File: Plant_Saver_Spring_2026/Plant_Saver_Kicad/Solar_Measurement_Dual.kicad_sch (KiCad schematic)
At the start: 9 parts, among them U14 MCP6234

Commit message: Resub from last
I forgot to save some of my changes from my last push
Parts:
- added C15: 0.1uF, Capacitor_THT:C_Disc_D4.7mm_W2.5mm_P5.00mm, symbol Device:C
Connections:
- net Vcc: now also C15.1; no longer U14.4 (V+)
- net Vmeas1: now also U14.1, U14.2 (-)
- new net: C15.2, U14.4 (V+)
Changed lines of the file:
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@@
+	)
+	(junction
+		(at 165.1 50.8)
+		(diameter 0)
+		(color 0 0 0 0)
 	)
 	(junction
@@
 	(wire
 		(pts
+			(xy 93.98 53.34) (xy 97.79 53.34)
+		)
+		(stroke
+			(width 0)
+			(type default)
+		)
+	)
+	(wire
+		(pts
 			(xy 138.43 132.08) (xy 140.97 132.08)
 		)
@@
 	(wire
 		(pts
+			(xy 165.1 50.8) (xy 170.18 50.8)
+		)
+		(stroke
+			(width 0)
+			(type default)
+		)
+	)
+	(wire
+		(pts
 			(xy 115.57 53.34) (xy 115.57 66.04)
 		)
@@
 	(wire
 		(pts
-			(xy 95.25 53.34) (xy 97.79 53.34)
+			(xy 82.55 53.34) (xy 86.36 53.34)
 		)
 		(stroke
@@
 	(hierarchical_label "Vcc"
 		(shape input)
-		(at 95.25 53.34 180)
+		(at 82.55 53.34 180)
 		(effects
 			(font
@@
 					(unit 1)
 				)
+			)
+		)
+	)
+	(symbol
+		(lib_id "Device:C")
+		(at 90.17 53.34 90)
+		(unit 1)
+		(exclude_from_sim no)
+		(in_bom yes)
+		(on_board yes)
+		(dnp no)
+		(property "Reference" "C15"
+			(at 88.9 50.038 0)
+			(effects
+				(font
+					(size 1.27 1.27)
+				)
+				(justify left)
+			)
+		)
+		(property "Value" "0.1uF"
+			(at 91.44 50.038 0)
+			(effects
+				(font
+					(size 1.27 1.27)
+				)
+				(justify left)
+			)
+		)
+		(property "Footprint" "Capacitor_THT:C_Disc_D4.7mm_W2.5mm_P5.00mm"
+			(at 93.98 52.3748 0)
+			(effects
+				(font
+					(size 1.27 1.27)
+				)
+				(hide yes)
+			)
+		)
+		(property "Datasheet" "~"
+			(at 90.17 53.34 0)
+			(effects
+				(font
+					(size 1.27 1.27)
+				)
+				(hide yes)
+			)
+		)
+		(property "Description" "Unpolarized capacitor"
+			(at 90.17 53.34 0)
+			(effects
+				(font
+					(size 1.27 1.27)
+				)
+				(hide yes)
+			)
+		)
+		(pin "1"
+		)
+		(pin "2"
+		)
+		(instances
+			(project "Plant_Saver_Kicad"
+				(path "/7f244634-d37a-4ff0-ba36-8027330ab1bd/9d841e6d-e3b2-48a8-9c06-32c643c2cc22"
+					(reference "C15")
+					(unit 1)
+				)

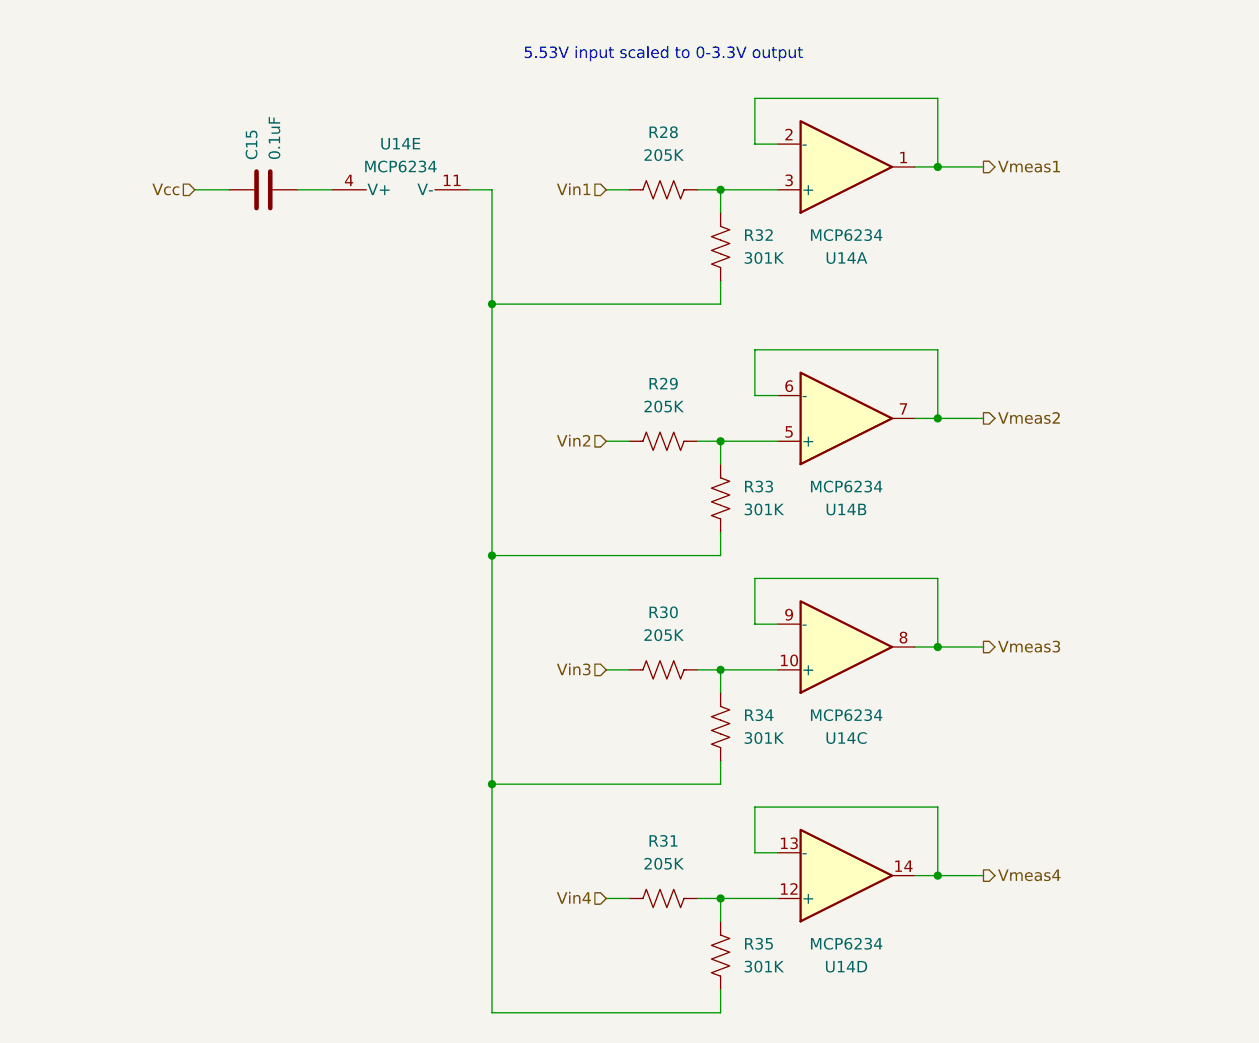
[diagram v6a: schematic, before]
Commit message: Refined PCB layout
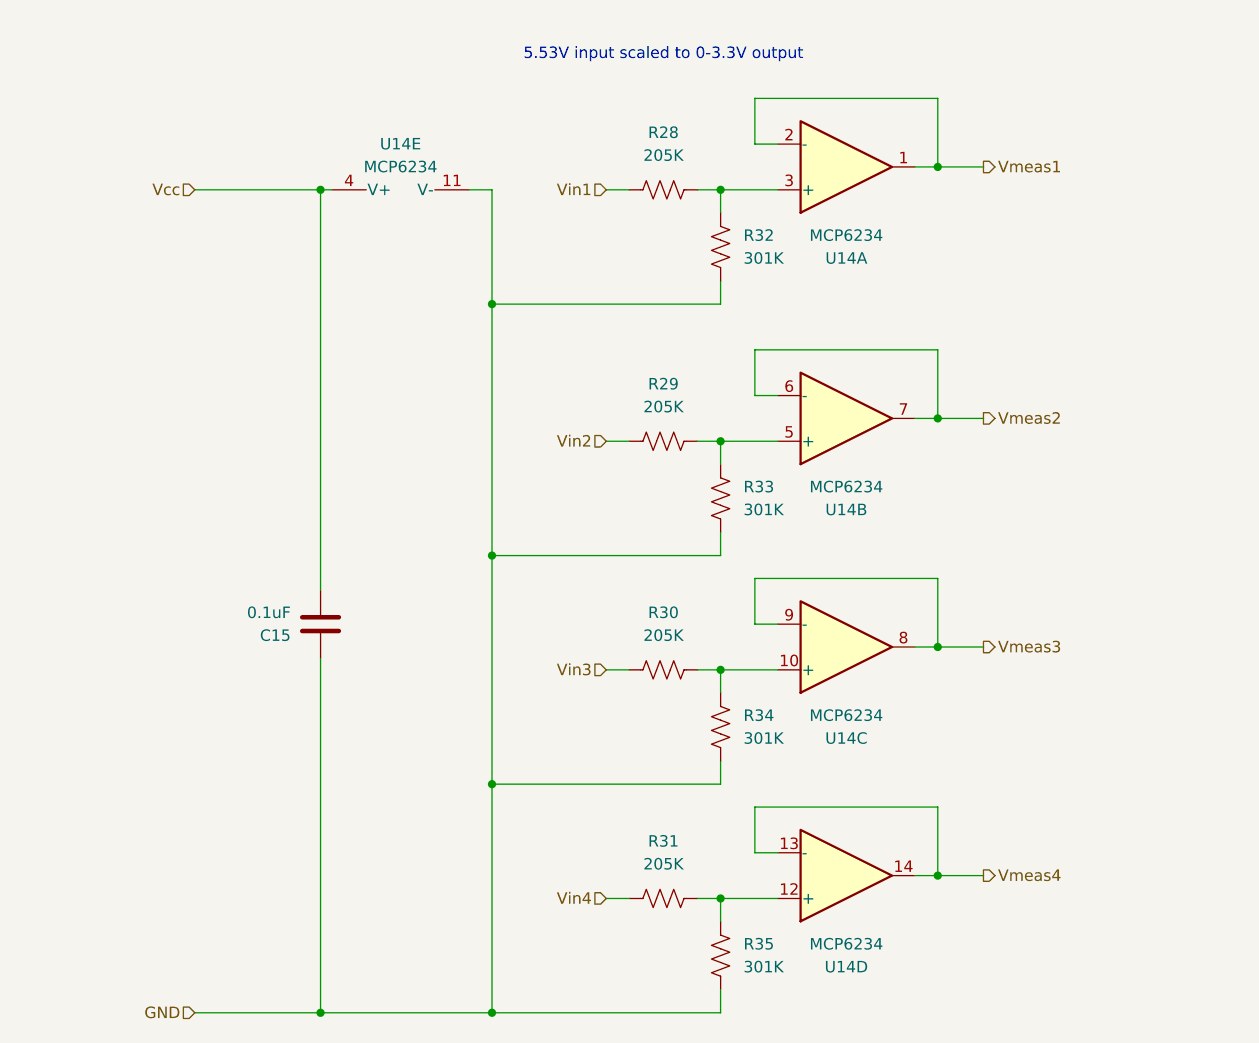
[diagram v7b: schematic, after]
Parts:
- C15: footprint Capacitor_THT:C_Disc_D4.7mm_W2.5mm_P5.00mm -> Capacitor_SMD:C_1206_3216Metric_Pad1.33x1.80mm_HandSolder; Field5 (none) -> CL31A106KBHNNNE
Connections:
- net Vcc: now also C15.2, U14.4 (V+); no longer C15.1
- net GND: now reaches R32.1, R33.1, R34.1, R35.1, U14.11 (V-)
- net GND: now also C15.1
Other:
- moved on the sheet: C15
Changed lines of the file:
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@@
+	)
+	(junction
+		(at 115.57 144.78)
+		(diameter 0)
+		(color 0 0 0 0)
 	)
 	(junction
@@
 	)
 	(junction
+		(at 96.52 144.78)
+		(diameter 0)
+		(color 0 0 0 0)
+	)
+	(junction
 		(at 165.1 129.54)
+		(diameter 0)
+		(color 0 0 0 0)
+	)
+	(junction
+		(at 96.52 53.34)
 		(diameter 0)
 		(color 0 0 0 0)
@@
 	(wire
 		(pts
-			(xy 93.98 53.34) (xy 97.79 53.34)
-		)
-		(stroke
-			(width 0)
-			(type default)
-		)
-	)
-	(wire
-		(pts
 			(xy 138.43 132.08) (xy 140.97 132.08)
 		)
@@
 	(wire
 		(pts
+			(xy 96.52 53.34) (xy 97.79 53.34)
+		)
+		(stroke
+			(width 0)
+			(type default)
+		)
+	)
+	(wire
+		(pts
 			(xy 165.1 43.18) (xy 165.1 50.8)
 		)
@@
 	(wire
 		(pts
+			(xy 96.52 144.78) (xy 115.57 144.78)
+		)
+		(stroke
+			(width 0)
+			(type default)
+		)
+	)
+	(wire
+		(pts
 			(xy 147.32 127) (xy 144.78 127)
 		)
@@
 	(wire
 		(pts
-			(xy 82.55 53.34) (xy 86.36 53.34)
+			(xy 82.55 53.34) (xy 96.52 53.34)
 		)
 		(stroke
@@
 	(wire
 		(pts
+			(xy 96.52 53.34) (xy 96.52 97.79)
+		)
+		(stroke
+			(width 0)
+			(type default)
+		)
+	)
+	(wire
+		(pts
 			(xy 140.97 132.08) (xy 147.32 132.08)
 		)
@@
 	(wire
 		(pts
+			(xy 82.55 144.78) (xy 96.52 144.78)
+		)
+		(stroke
+			(width 0)
+			(type default)
+		)
+	)
+	(wire
+		(pts
 			(xy 165.1 50.8) (xy 162.56 50.8)
 		)
@@
 		(pts
 			(xy 144.78 101.6) (xy 144.78 96.52)
+		)
+		(stroke
+			(width 0)
+			(type default)
+		)
+	)
+	(wire
+		(pts
+			(xy 96.52 105.41) (xy 96.52 144.78)
 		)
 		(stroke
@@
 		(shape input)
 		(at 128.27 132.08 180)
+		(effects
+			(font
+				(size 1.27 1.27)
+			)
+			(justify right)
+		)
+	)
+	(hierarchical_label "GND"
+		(shape input)
+		(at 82.55 144.78 180)
 		(effects
 			(font
@@
 	(symbol
 		(lib_id "Device:C")
-		(at 90.17 53.34 90)
+		(at 96.52 101.6 180)
 		(unit 1)
 		(exclude_from_sim no)
@@
 		(dnp no)
 		(property "Reference" "C15"
-			(at 88.9 50.038 0)
+			(at 93.218 102.87 0)
 			(effects
 				(font
@@
 		)
 		(property "Value" "0.1uF"
-			(at 91.44 50.038 0)
+			(at 93.218 100.33 0)
 			(effects
 				(font
@@
 			)
 		)
-		(property "Footprint" "Capacitor_THT:C_Disc_D4.7mm_W2.5mm_P5.00mm"
-			(at 93.98 52.3748 0)
+		(property "Footprint" "Capacitor_SMD:C_1206_3216Metric_Pad1.33x1.80mm_HandSolder"
+			(at 95.5548 97.79 0)
 			(effects
 				(font
@@
 		)
 		(property "Datasheet" "~"
-			(at 90.17 53.34 0)
+			(at 96.52 101.6 0)
 			(effects
 				(font
@@
 		)
 		(property "Description" "Unpolarized capacitor"
-			(at 90.17 53.34 0)
-			(effects
-				(font
+			(at 96.52 101.6 0)
+			(effects
+				(font
+					(size 1.27 1.27)
+				)
+				(hide yes)
+			)
+		)
+		(property "Field5" "CL31A106KBHNNNE"
+			(at 96.52 101.6 0)
+			(effects
+				(font

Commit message: PCB Pre-Check complete
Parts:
- renumbered C15 to C13, R28 to R30, R29 to R31, R30 to R32, R31 to R33, R32 to R34, R33 to R35, R34 to R36, R35 to R37
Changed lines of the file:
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@@
 		(dnp no)
 		(fields_autoplaced yes)
-		(property "Reference" "R32"
+		(property "Reference" "R34"
 			(at 143.51 58.4199 0)
 			(effects
@@
 			(project "Plant_Saver_Kicad"
 				(path "/7f244634-d37a-4ff0-ba36-8027330ab1bd/9d841e6d-e3b2-48a8-9c06-32c643c2cc22"
-					(reference "R32")
+					(reference "R34")
 					(unit 1)
 				)
@@
 		(dnp no)
 		(fields_autoplaced yes)
-		(property "Reference" "R33"
+		(property "Reference" "R35"
 			(at 143.51 86.3599 0)
 			(effects
@@
 			(project "Plant_Saver_Kicad"
 				(path "/7f244634-d37a-4ff0-ba36-8027330ab1bd/9d841e6d-e3b2-48a8-9c06-32c643c2cc22"
-					(reference "R33")
+					(reference "R35")
 					(unit 1)
 				)
@@
 		(dnp no)
 		(fields_autoplaced yes)
-		(property "Reference" "R34"
+		(property "Reference" "R36"
 			(at 143.51 111.7599 0)
 			(effects
@@
 			(project "Plant_Saver_Kicad"
 				(path "/7f244634-d37a-4ff0-ba36-8027330ab1bd/9d841e6d-e3b2-48a8-9c06-32c643c2cc22"
-					(reference "R34")
+					(reference "R36")
 					(unit 1)
 				)
@@
 		(dnp no)
 		(fields_autoplaced yes)
-		(property "Reference" "R35"
+		(property "Reference" "R37"
 			(at 143.51 137.1599 0)
 			(effects
@@
 			(project "Plant_Saver_Kicad"
 				(path "/7f244634-d37a-4ff0-ba36-8027330ab1bd/9d841e6d-e3b2-48a8-9c06-32c643c2cc22"
-					(reference "R35")
+					(reference "R37")
 					(unit 1)
 				)
@@
 		(dnp no)
 		(fields_autoplaced yes)
-		(property "Reference" "R28"
+		(property "Reference" "R30"
 			(at 134.62 46.99 90)
 			(effects
@@
 			(project "Plant_Saver_Kicad"
 				(path "/7f244634-d37a-4ff0-ba36-8027330ab1bd/9d841e6d-e3b2-48a8-9c06-32c643c2cc22"
-					(reference "R28")
+					(reference "R30")
 					(unit 1)
 				)
@@
 		(dnp no)
 		(fields_autoplaced yes)
-		(property "Reference" "R31"
+		(property "Reference" "R33"
 			(at 134.62 125.73 90)
 			(effects
@@
 			(project "Plant_Saver_Kicad"
 				(path "/7f244634-d37a-4ff0-ba36-8027330ab1bd/9d841e6d-e3b2-48a8-9c06-32c643c2cc22"
-					(reference "R31")
+					(reference "R33")
 					(unit 1)
 				)
@@
 		(on_board yes)
 		(dnp no)
-		(property "Reference" "C15"
+		(property "Reference" "C13"
 			(at 93.218 102.87 0)
 			(effects
@@
 			(project "Plant_Saver_Kicad"
 				(path "/7f244634-d37a-4ff0-ba36-8027330ab1bd/9d841e6d-e3b2-48a8-9c06-32c643c2cc22"
-					(reference "C15")
+					(reference "C13")
 					(unit 1)
 				)
@@
 		(dnp no)
 		(fields_autoplaced yes)
-		(property "Reference" "R29"
+		(property "Reference" "R31"
 			(at 134.62 74.93 90)
 			(effects
@@
 			(project "Plant_Saver_Kicad"
 				(path "/7f244634-d37a-4ff0-ba36-8027330ab1bd/9d841e6d-e3b2-48a8-9c06-32c643c2cc22"
-					(reference "R29")
+					(reference "R31")
 					(unit 1)
 				)
@@
 		(dnp no)
 		(fields_autoplaced yes)
-		(property "Reference" "R30"
+		(property "Reference" "R32"
 			(at 134.62 100.33 90)
 			(effects
@@
 			(project "Plant_Saver_Kicad"
 				(path "/7f244634-d37a-4ff0-ba36-8027330ab1bd/9d841e6d-e3b2-48a8-9c06-32c643c2cc22"
-					(reference "R30")
+					(reference "R32")
 					(unit 1)
 				)
